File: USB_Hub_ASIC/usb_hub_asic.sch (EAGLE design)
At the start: 105 parts, among them J1 CONN_RCPT_USB3.0_TYPEB_9POS_R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, J2 CONN_RCPT_USB3.0_TYPEA_9POS_R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, J3 CONN_RCPT_USB3.0_TYPEA_9POS_R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, J4 CONN_RCPT_USB3.0_TYPEA_9POS_R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, J5 CONN_RCPT_USB3.0_TYPEA_9POS_R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, Q1 26M, U1 IC_MCP1603LT-330_3.3V_500MA_B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, U2 IC_CYUSB3314_QUAD_USB3.0_HUB, U3 IC_LM3674MF-1.2/NOPB_1.2V_600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

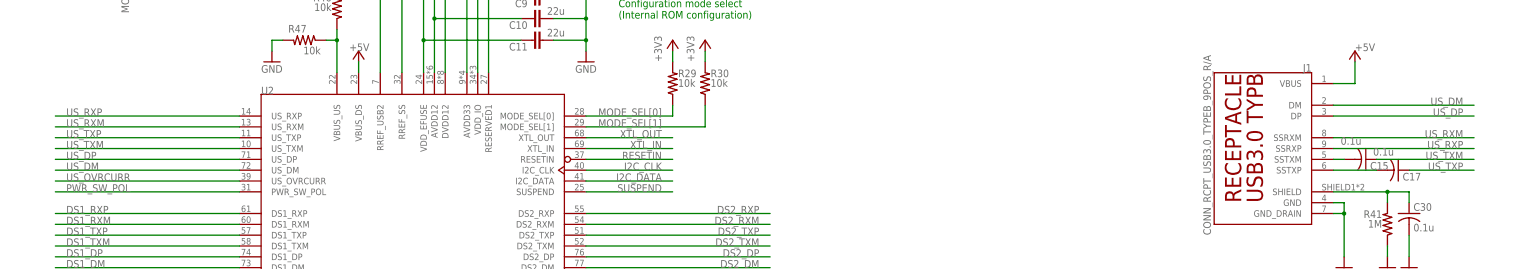
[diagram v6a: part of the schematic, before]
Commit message: Power plane routing for chip
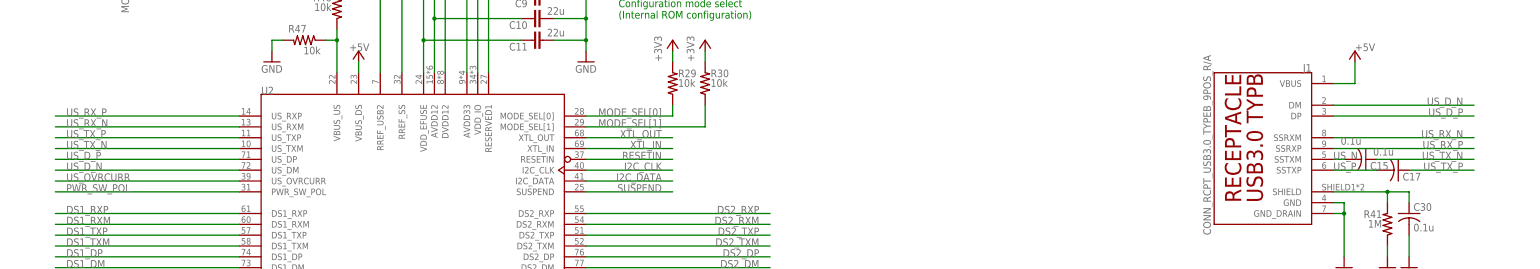
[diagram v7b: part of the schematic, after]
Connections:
- net N$5 renamed US_N
- net N$6 renamed US_P
- net US_DM renamed US_D_N
- net US_DP renamed US_D_P
- net US_RXM renamed US_RX_N
- net US_RXP renamed US_RX_P
- net US_TXM renamed US_TX_N
- net US_TXP renamed US_TX_P
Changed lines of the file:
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@@
 </busses>
 <nets>
-<net name="US_RXP" class="0">
+<net name="US_RX_P" class="0">
 <segment>
 <pinref part="U2" gate="G$1" pin="US_RXP"/>
@@
 </segment>
 </net>
-<net name="US_RXM" class="0">
-<segment>
-<pinref part="U2" gate="G$1" pin="US_RXM"/>
-<wire x1="55.88" y1="104.14" x2="12.7" y2="104.14" width="0.1524" layer="91"/>
-<label x="15.24" y="104.14" size="1.778" layer="95"/>
-</segment>
-<segment>
-<wire x1="312.42" y1="101.6" x2="345.44" y2="101.6" width="0.1524" layer="91"/>
-<label x="342.9" y="101.6" size="1.778" layer="95" rot="MR0"/>
-<pinref part="J1" gate="G$1" pin="SSRXM"/>
-</segment>
-</net>
-<net name="US_TXP" class="0">
+<net name="US_TX_P" class="0">
 <segment>
 <pinref part="U2" gate="G$1" pin="US_TXP"/>
@@
 <wire x1="330.2" y1="93.98" x2="345.44" y2="93.98" width="0.1524" layer="91"/>
 <label x="342.9" y="93.98" size="1.778" layer="95" rot="MR0"/>
-</segment>
-</net>
-<net name="US_TXM" class="0">
-<segment>
-<pinref part="U2" gate="G$1" pin="US_TXM"/>
-<wire x1="55.88" y1="99.06" x2="12.7" y2="99.06" width="0.1524" layer="91"/>
-<label x="15.24" y="99.06" size="1.778" layer="95"/>
-</segment>
-<segment>
-<pinref part="C15" gate="G$1" pin="1"/>
-<wire x1="322.58" y1="96.52" x2="345.44" y2="96.52" width="0.1524" layer="91"/>
-<label x="342.9" y="96.52" size="1.778" layer="95" rot="MR0"/>
-</segment>
-</net>
-<net name="US_DP" class="0">
-<segment>
-<pinref part="U2" gate="G$1" pin="US_DP"/>
-<wire x1="55.88" y1="96.52" x2="12.7" y2="96.52" width="0.1524" layer="91"/>
-<label x="15.24" y="96.52" size="1.778" layer="95"/>
-</segment>
-<segment>
-<wire x1="312.42" y1="106.68" x2="345.44" y2="106.68" width="0.1524" layer="91"/>
-<label x="342.9" y="106.68" size="1.778" layer="95" rot="MR0"/>
-<pinref part="J1" gate="G$1" pin="DP"/>
-</segment>
-</net>
-<net name="US_DM" class="0">
-<segment>
-<pinref part="U2" gate="G$1" pin="US_DM"/>
-<wire x1="55.88" y1="93.98" x2="12.7" y2="93.98" width="0.1524" layer="91"/>
-<label x="15.24" y="93.98" size="1.778" layer="95"/>
-</segment>
-<segment>
-<wire x1="312.42" y1="109.22" x2="345.44" y2="109.22" width="0.1524" layer="91"/>
-<label x="342.9" y="109.22" size="1.778" layer="95" rot="MR0"/>
-<pinref part="J1" gate="G$1" pin="DM"/>
 </segment>
 </net>
@@
 </segment>
 </net>
-<net name="N$5" class="0">
+<net name="US_N" class="0">
 <segment>
 <pinref part="C15" gate="G$1" pin="2"/>
 <wire x1="314.96" y1="96.52" x2="312.42" y2="96.52" width="0.1524" layer="91"/>
 <pinref part="J1" gate="G$1" pin="SSTXM"/>
-</segment>
-</net>
-<net name="N$6" class="0">
+<label x="312.42" y="96.52" size="1.778" layer="95"/>
+</segment>
+</net>
+<net name="US_P" class="0">
 <segment>
 <pinref part="C17" gate="G$1" pin="2"/>
 <wire x1="312.42" y1="93.98" x2="322.58" y2="93.98" width="0.1524" layer="91"/>
 <pinref part="J1" gate="G$1" pin="SSTXP"/>
+<label x="312.42" y="93.98" size="1.778" layer="95"/>
 </segment>
 </net>
@@
 </segment>
 </net>
+<net name="US_D_P" class="0">
+<segment>
+<pinref part="U2" gate="G$1" pin="US_DP"/>
+<wire x1="55.88" y1="96.52" x2="12.7" y2="96.52" width="0.1524" layer="91"/>
+<label x="15.24" y="96.52" size="1.778" layer="95"/>
+</segment>
+<segment>
+<wire x1="312.42" y1="106.68" x2="345.44" y2="106.68" width="0.1524" layer="91"/>
+<label x="342.9" y="106.68" size="1.778" layer="95" rot="MR0"/>
+<pinref part="J1" gate="G$1" pin="DP"/>
+</segment>
+</net>
+<net name="US_D_N" class="0">
+<segment>
+<pinref part="U2" gate="G$1" pin="US_DM"/>
+<wire x1="55.88" y1="93.98" x2="12.7" y2="93.98" width="0.1524" layer="91"/>
+<label x="15.24" y="93.98" size="1.778" layer="95"/>
+</segment>
+<segment>
+<wire x1="312.42" y1="109.22" x2="345.44" y2="109.22" width="0.1524" layer="91"/>
+<label x="342.9" y="109.22" size="1.778" layer="95" rot="MR0"/>
+<pinref part="J1" gate="G$1" pin="DM"/>
+</segment>
+</net>
+<net name="US_RX_N" class="0">
+<segment>
+<pinref part="U2" gate="G$1" pin="US_RXM"/>
+<wire x1="55.88" y1="104.14" x2="12.7" y2="104.14" width="0.1524" layer="91"/>
+<label x="15.24" y="104.14" size="1.778" layer="95"/>
+</segment>
+<segment>
+<wire x1="312.42" y1="101.6" x2="345.44" y2="101.6" width="0.1524" layer="91"/>
+<label x="342.9" y="101.6" size="1.778" layer="95" rot="MR0"/>
+<pinref part="J1" gate="G$1" pin="SSRXM"/>
+</segment>
+</net>
+<net name="US_TX_N" class="0">
+<segment>
+<pinref part="U2" gate="G$1" pin="US_TXM"/>
+<wire x1="55.88" y1="99.06" x2="12.7" y2="99.06" width="0.1524" layer="91"/>
+<label x="15.24" y="99.06" size="1.778" layer="95"/>
+</segment>
+<segment>
+<pinref part="C15" gate="G$1" pin="1"/>
+<wire x1="322.58" y1="96.52" x2="345.44" y2="96.52" width="0.1524" layer="91"/>
+<label x="342.9" y="96.52" size="1.778" layer="95" rot="MR0"/>
+</segment>
+</net>

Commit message: Component selection and a bit more placement
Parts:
- C1, C3, C4: device rcl:CPOL-USSANYO_SMD_E12 -> rcl:C-USC0603
- C10, C11, C12, C13, C6, C7, C8, C9: device SparkFun-Capacitors:CAP-0603 -> rcl:C-USC0603
- C14, C16, C20, C21: device rcl:CPOL-USSANYO_SMD_E12 -> rcl:C-USC1210K
- C18, C19, C22, C23, C24, C25, C28, C29, C30, C31, C32, C33, C34: device rcl:C-USC0805 -> rcl:C-USC0603
- C5: device rcl:CPOL-USSANYO_SMD_E12 -> rcl:C-USC0805
- L1: device rcl:L-USCEP125 -> USB_Hub_ASIC:L_4.7UH_1.5A_SMD_1212(3030METRIC)
- L2: device rcl:L-USCEP125 -> USB_Hub_ASIC:L_2.2UH_1.3A_SMD_0805(2012METRIC)
- Q1: device crystal:CRYSTALHC49S -> USB_Hub_ASIC:XTAL_26MHZ_4-SMD_ECX-42
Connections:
- net DS1_DM renamed DS1_D_N
- net DS1_DP renamed DS1_D_P
- net DS1_RXM renamed DS1_RX_N
- net DS1_RXP renamed DS1_RX_P
- net DS1_TXM renamed DS1_TX_N
- net DS1_TXP renamed DS1_TX_P
- net DS2_DM renamed DS2_D_N
- net DS2_DP renamed DS2_D_P
- net DS2_RXM renamed DS2_RX_N
- net DS2_RXP renamed DS2_RX_P
- net DS2_TXM renamed DS2_TX_N
- net DS2_TXP renamed DS2_TX_P
- net DS3_DM renamed DS3_D_N
- net DS3_DP renamed DS3_D_P
- net DS3_RXM renamed DS3_RX_N
- net DS3_RXP renamed DS3_RX_P
- net DS3_TXM renamed DS3_TX_N
- net DS3_TXP renamed DS3_TX_P
- net DS4_DM renamed DS4_D_N
- net DS4_DP renamed DS4_D_P
- net DS4_RXM renamed DS4_RX_N
- net DS4_RXP renamed DS4_RX_P
- net DS4_TXM renamed DS4_TX_N
- net DS4_TXP renamed DS4_TX_P
- net N$1 renamed D1_N
- net N$10 renamed D2_P
- net N$13 renamed D3_N
- net N$14 renamed D3_P
- net N$17 renamed D4_N
- net N$18 renamed D4_P
- net N$2 renamed D1_P
- net N$9 renamed D2_N
- removed net N$3: C14.+, C16.+, C20.+, C21.+, J2.VBUS, J3.VBUS, J4.VBUS, J5.VBUS
- net +1V2: now also C5.1; no longer C5.+
- net +3V3: now also C3.1; no longer C3.+
- net +5V: now also C1.1, C14.1, C16.1, C20.1, C21.1, C4.1, J2.VBUS, J3.VBUS, J4.VBUS, J5.VBUS; no longer C1.+, C4.+
- net GND: now also C1.2, C14.2, C16.2, C20.2, C21.2, C3.2, C4.2, C5.2, Q1.GND; no longer C1.-, C14.-, C16.-, C20.-, C21.-, C3.-, C4.-, C5.-
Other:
- moved on the sheet: C10, C11, C12, C13, C6, C7, C8, C9
